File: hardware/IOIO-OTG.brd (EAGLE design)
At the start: 68.6 x 30.5 mm, 59 parts, among them Q1 IRLML2244, Q2 2N7002PW, Q3 AO3404A, U1 PIC24FJ256GB206, U14 SWITCH_SPDT, U2 TPS62133RGTT, U3 VREG_MIC5216

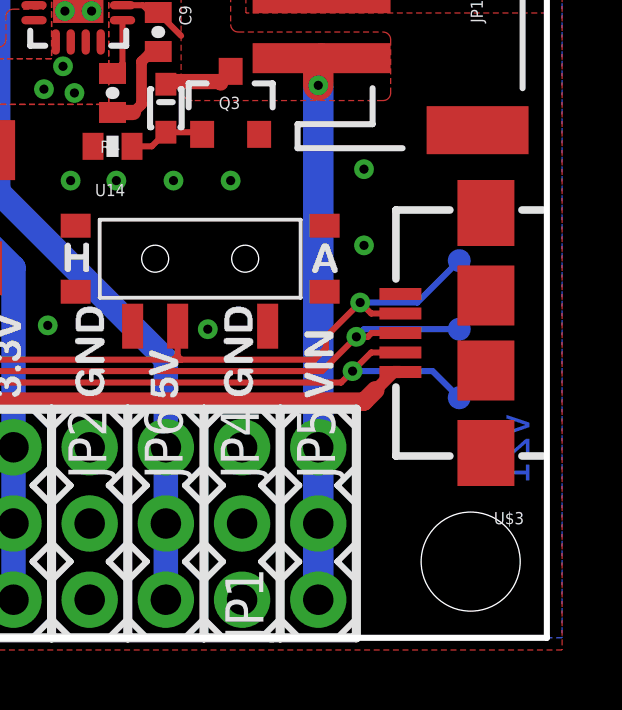
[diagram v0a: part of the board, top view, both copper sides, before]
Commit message: Switch USB connector to part with mounting bosses
Also included an anchor polygon to strengthen mounting pads.
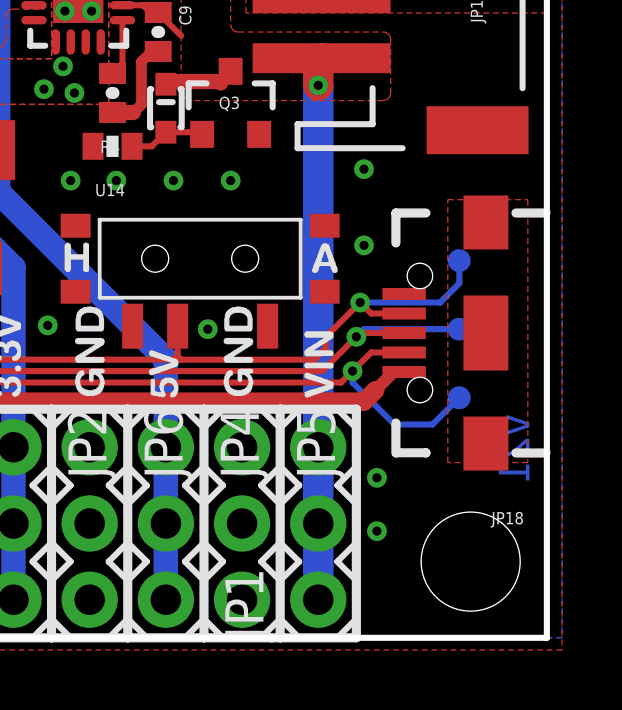
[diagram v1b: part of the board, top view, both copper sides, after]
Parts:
- removed U$3: 10104111-0001LF, SparkFun-Connectors:USB-AB-MICRO-SMD
- added JP18: (no value), SparkFun-Connectors:USB-B-MICRO-SMD_V03
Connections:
- new net ANCHOR1: JP18.SHIELD1, JP18.SHIELD2, JP18.SHIELD3
- net D+: now also JP18.D+1; no longer U$3.D+
- net D-: now also JP18.D-1; no longer U$3.D-
- net GND: now also JP18.GND1; no longer U$3.GND
- net USBID: now also JP18.ID1; no longer U$3.ID
- net VBUS: now also JP18.VBUS1; no longer U$3.VBUS
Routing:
- net D-: track 49.6 -> 50.7 mm
- net USBID: track 45.7 -> 46.3 mm
- net GND: vias 79 -> 81
- added copper zone on layer 1, net ANCHOR1

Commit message: Moved OSHW logo to proper device
Also moved measures to measure layer and changed units to inches
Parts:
- added LOGO1: OSHW-LOGOS, SparkFun-Aesthetics:OSHW-LOGO-S

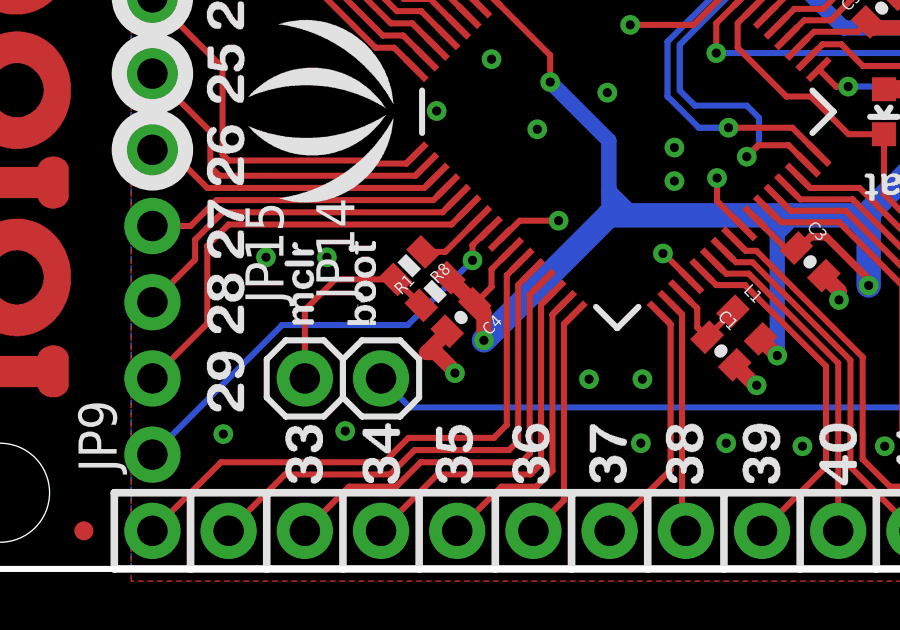
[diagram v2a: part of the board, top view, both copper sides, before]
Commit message: Moved R1, R8, C4 to proper 0603 packages
All three components had to move slightly. This will require updating
their x/y coordinates.
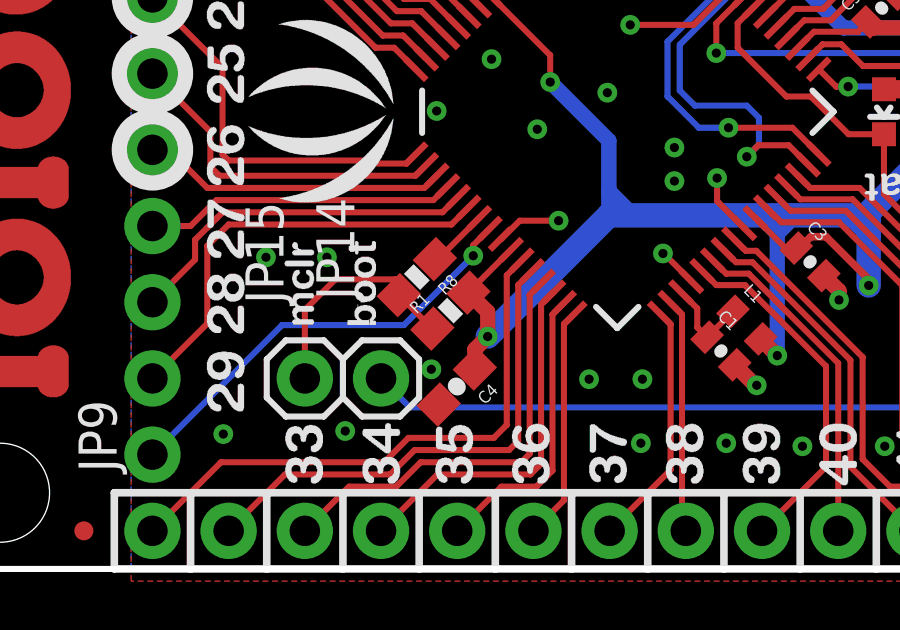
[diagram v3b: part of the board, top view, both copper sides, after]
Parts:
- C4: device SparkFun:0402-CAP -> SparkFun-Capacitors:0603-CAP
- R1: value 10k -> 10K; device SparkFun:0402-RES -> SparkFun-Resistors:0603-RES
- R8: device SparkFun:0402-RES -> SparkFun-Resistors:0603-RES
- moved C4 2.31 mm to (17.8, 6.08)
- moved R1 0.81 mm to (17.6, 8.61)
- moved R8 0.46 mm to (16.4, 9.73)
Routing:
- net GND: track 45.5 -> 43.3 mm
- net P7: track 6.95 -> 7.84 mm
